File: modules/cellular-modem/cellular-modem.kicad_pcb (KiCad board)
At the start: 2 copper layers, 42.8 x 71.1 mm, 21 parts, among them J1 MM60-mini-PCIe, J2 MM60-EZH059-B5-R650, U1 TXV0108RGYR, U2 TXV0108RGYR, U3 TXV0108RGYR, U4 TPS631000DRLR, U5 TPS631000DRLR

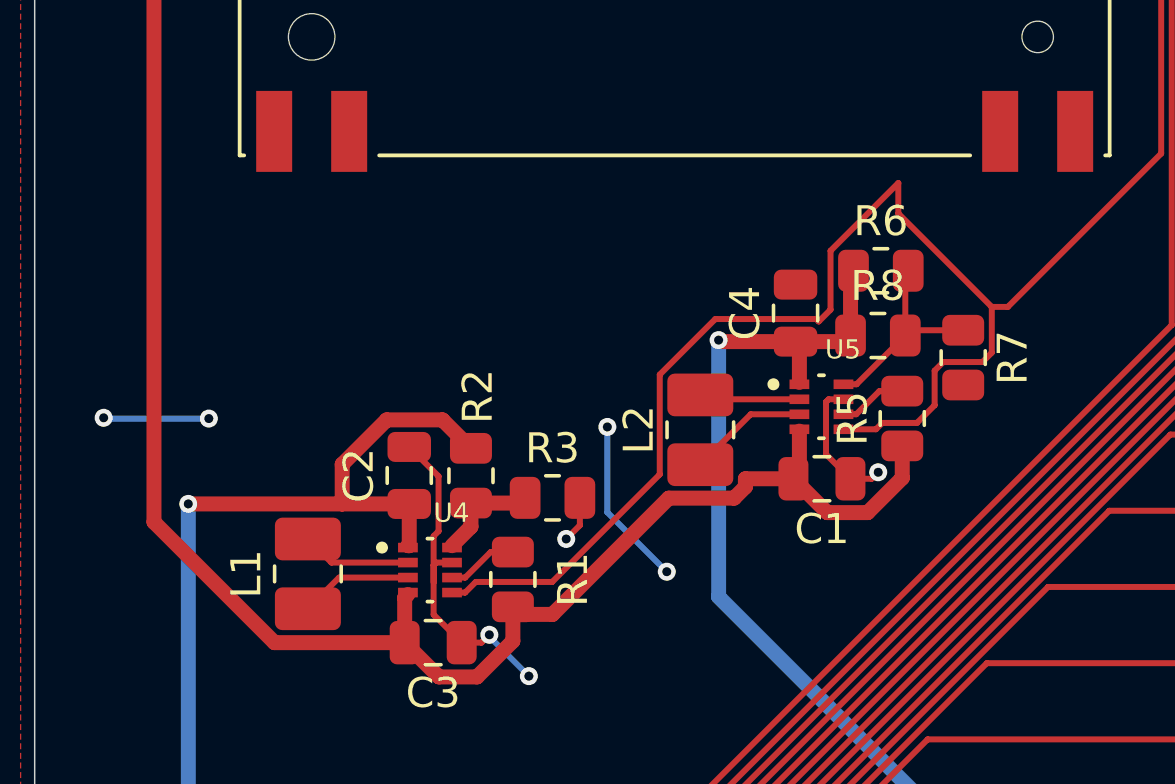
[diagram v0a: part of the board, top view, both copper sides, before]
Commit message: add jumpers for isolating 1.8V and 3.3V regulators
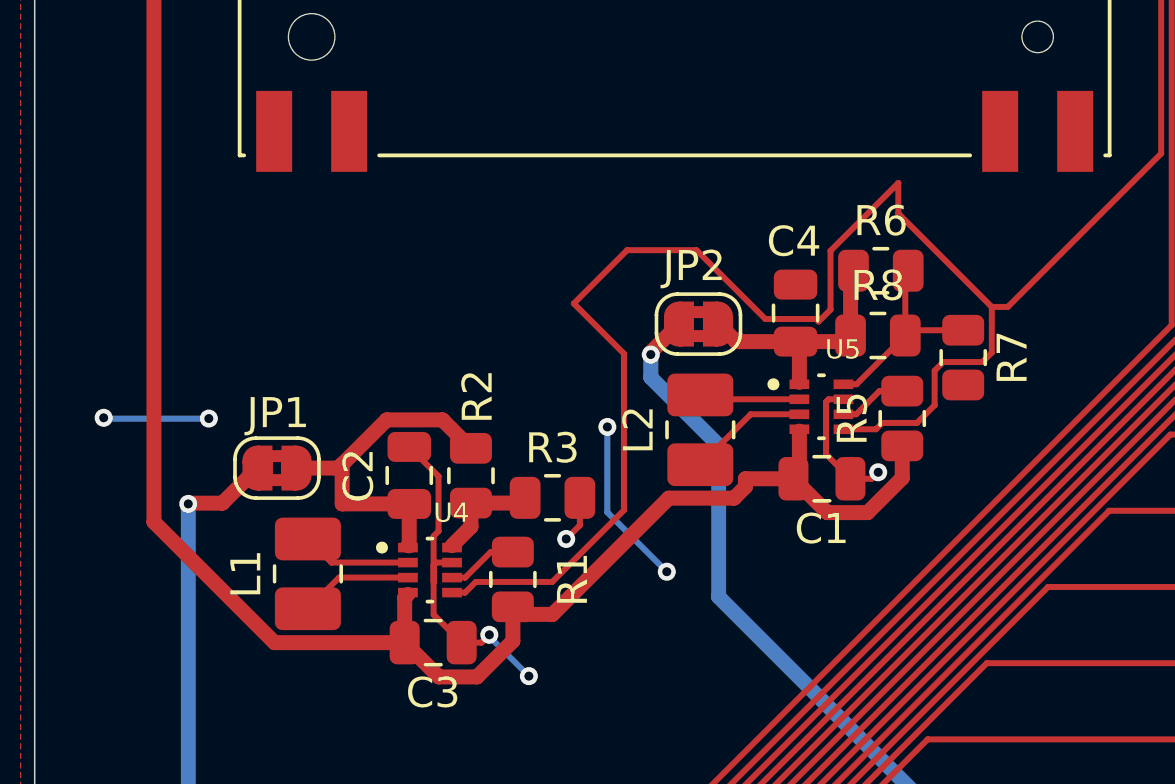
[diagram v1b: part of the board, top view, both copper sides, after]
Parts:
- added JP1: Jumper_2_Bridged, Jumper:SolderJumper-2_P1.3mm_Bridged2Bar_RoundedPad1.0x1.5mm, F.Cu at (75.9, 58.3)
- added JP2: Jumper_2_Bridged, Jumper:SolderJumper-2_P1.3mm_Bridged2Bar_RoundedPad1.0x1.5mm, F.Cu at (89.9, 53.5)
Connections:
- C2 pad 1: 3V3 -> Net-(JP1-A)
- C4 pad 1: 1V8 -> Net-(JP2-A)
- R2 pad 1: 3V3 -> Net-(JP1-A)
- R6 pad 1: 1V8 -> Net-(JP2-A)
- R8 pad 1: 1V8 -> Net-(JP2-A)
- U4 pad 1: 3V3 -> Net-(JP1-A)
- U5 pad 1: 1V8 -> Net-(JP2-A)
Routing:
- net 3V3: track 138.6 -> 125.6 mm
- net Net-(JP1-A): track 0.00 -> 12.4 mm
- net Net-(JP2-A): track 0.00 -> 8.56 mm
- net 1V8: track 77.2 -> 70.7 mm
- net EN: track 57.7 -> 64.0 mm

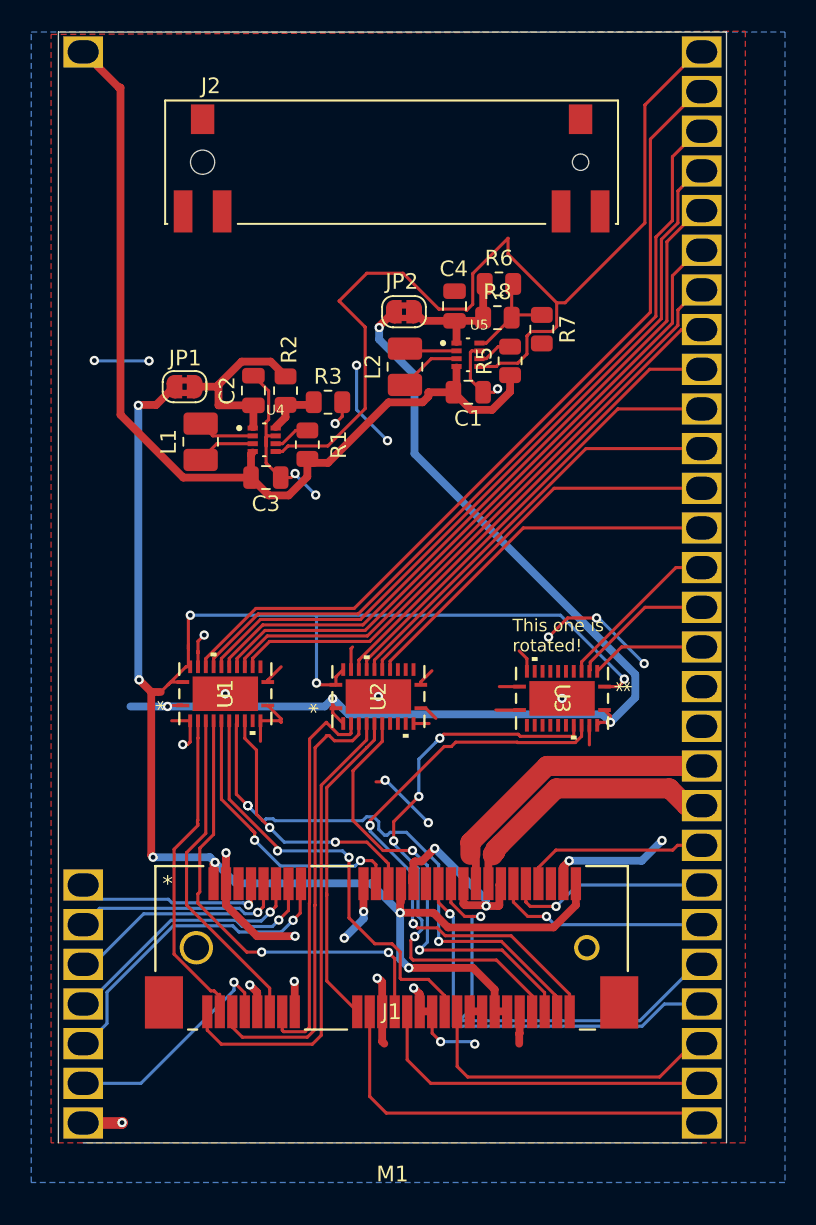
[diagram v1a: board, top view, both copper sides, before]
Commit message: label all pads
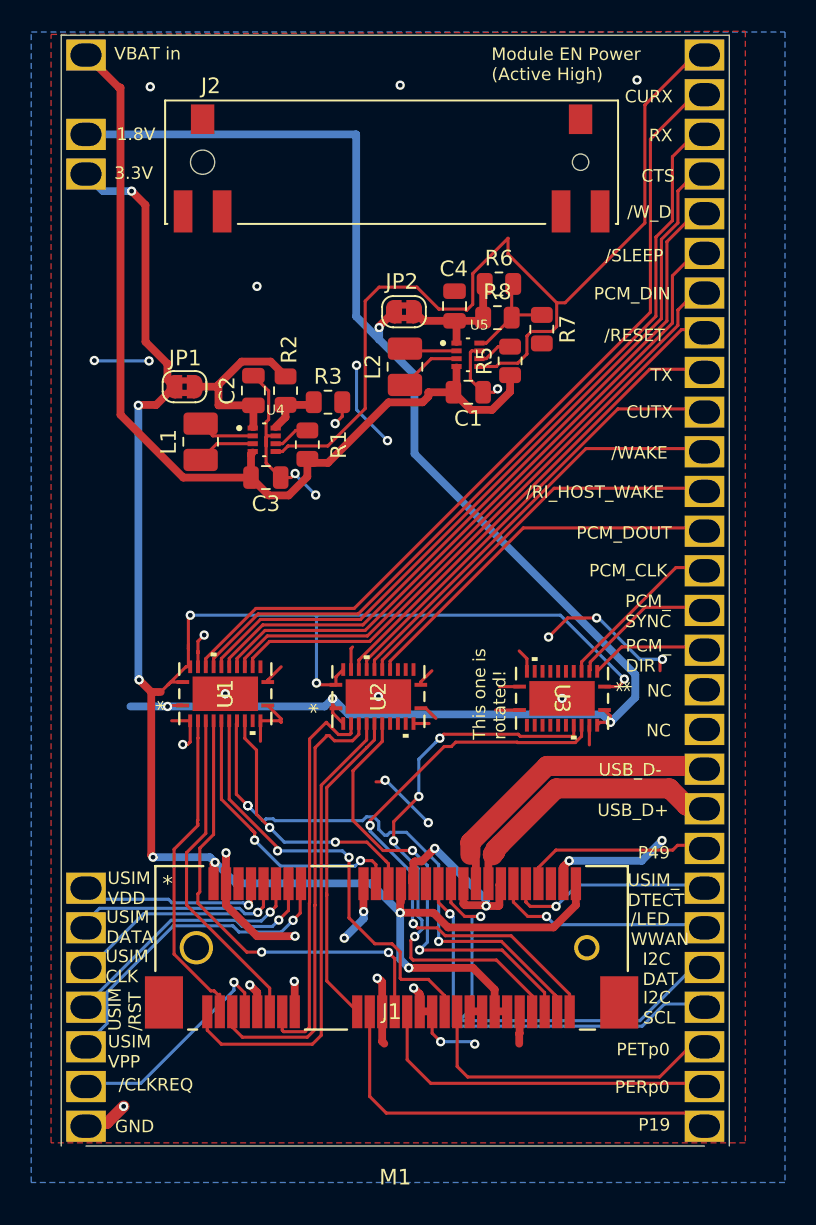
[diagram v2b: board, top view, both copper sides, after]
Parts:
- M1: footprint MegaCastle:MegaCastle2x28-Module-I36.0x66.3-M800007FFFFFFFF-NIBBLE -> MegaCastle:MegaCastle2x28-Module-I36.0x66.3-MB00007FFFFFFFF-NIBBLE
- moved M1 0.27 mm to (89.3, 71.3)
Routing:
- net 1V8: track 70.7 -> 101.8 mm
- net 3V3: track 125.6 -> 142.6 mm, vias 9 -> 10
- net EN: track 64.0 -> 60.9 mm
- net GND: track 117.0 -> 119.2 mm, vias 33 -> 37
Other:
- board text added: "/CLKREQ"
- board text added: "/LED WWAN"
- board text added: "/RESET"
- board text added: "/RI_HOST_WAKE"
- board text added: "/SLEEP"
- board text added: "/WAKE"
- board text added: "/W_D"
- board text added: "1.8V"
- board text added: "3.3V"
- board text added: "CTS"
- board text added: "CURX"
- board text added: "CUTX"
- board text added: "GND"
- board text added: "I2C DAT"
- board text added: "I2C SCL"
- board text added: "Module EN Power (Active High)"
- board text added: "NC"
- board text added: "P19"
- board text added: "P49"
- board text added: "PCM_ DIR"
- board text added: "PCM_ SYNC"
- board text added: "PCM_CLK"
- board text added: "PCM_DIN"
- board text added: "PCM_DOUT"
- board text added: "PERp0"
- board text added: "PETp0"
- board text added: "RX"
- board text added: "TX"
- board text added: "USB_D+"
- board text added: "USB_D-"
- board text added: "USIM /RST"
- board text added: "USIM CLK"
- board text added: "USIM DATA"
- board text added: "USIM VDD"
- board text added: "USIM VPP"
- board text added: "USIM_ DTECT"
- board text added: "VBAT in"

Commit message: begin work on SIM / SD card module
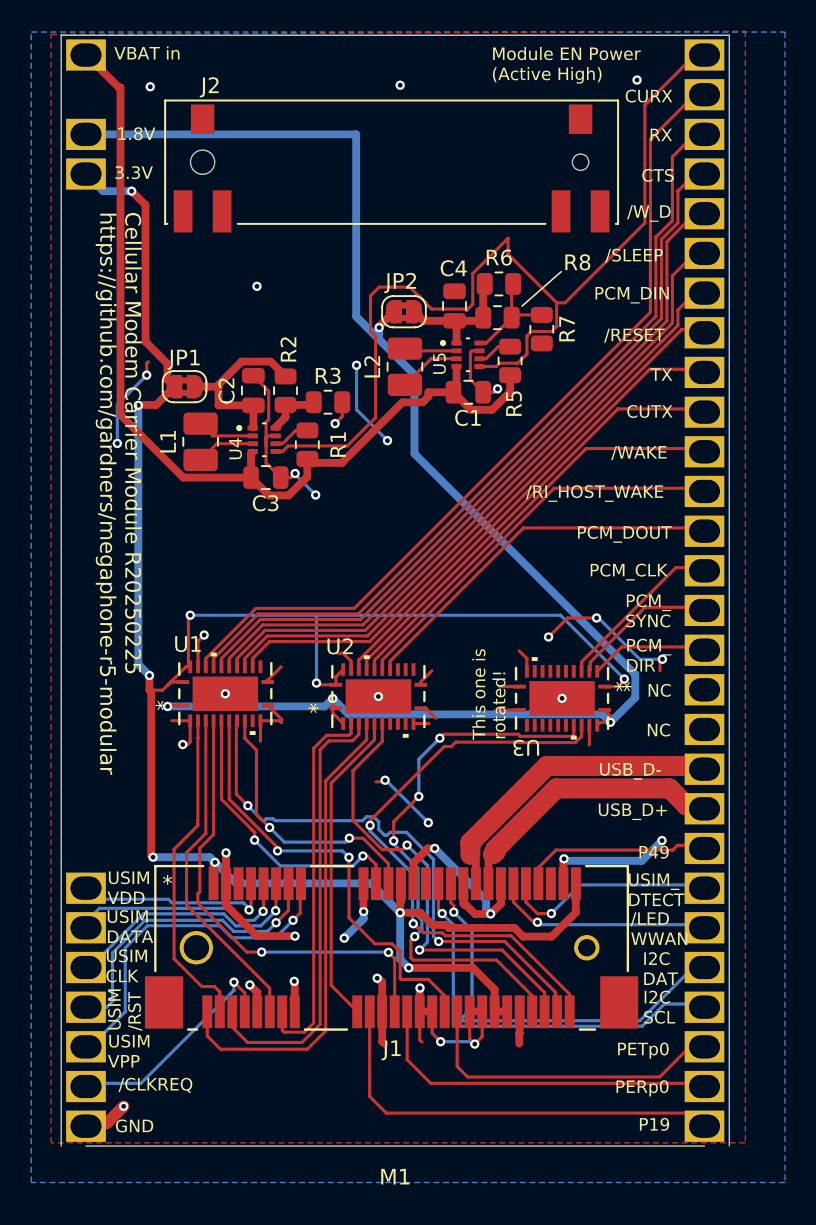
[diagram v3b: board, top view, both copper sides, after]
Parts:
- J1: value MM60-mini-PCIe -> MM60-52B1-E1-R650
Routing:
- net GND: track 119.2 -> 129.0 mm
- net 1V8: track 101.8 -> 99.4 mm
- net /USIM_RESET: track 17.7 -> 20.0 mm
- net USIM_VPP: track 20.8 -> 22.5 mm
- net I2C_DATA_1V8: track 28.1 -> 26.7 mm
- net /UART_TX_1V8_OUT: track 25.6 -> 24.5 mm
- net EN: track 60.9 -> 61.9 mm
- net USIM_VDD: track 12.6 -> 13.1 mm
- net USIM_DATA: track 13.8 -> 14.3 mm
- net /PCM_DIN_1V8_IN: track 35.2 -> 35.3 mm, vias 3 -> 2
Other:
- board text added: "Cellular Modem Carrier Module R20250225 https://github.com/gardners/megaphone-r5-modular"
